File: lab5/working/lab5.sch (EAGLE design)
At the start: 53 parts, among them J1 ISP, U1 ATMEGA128RFA1, Y1 16MHz

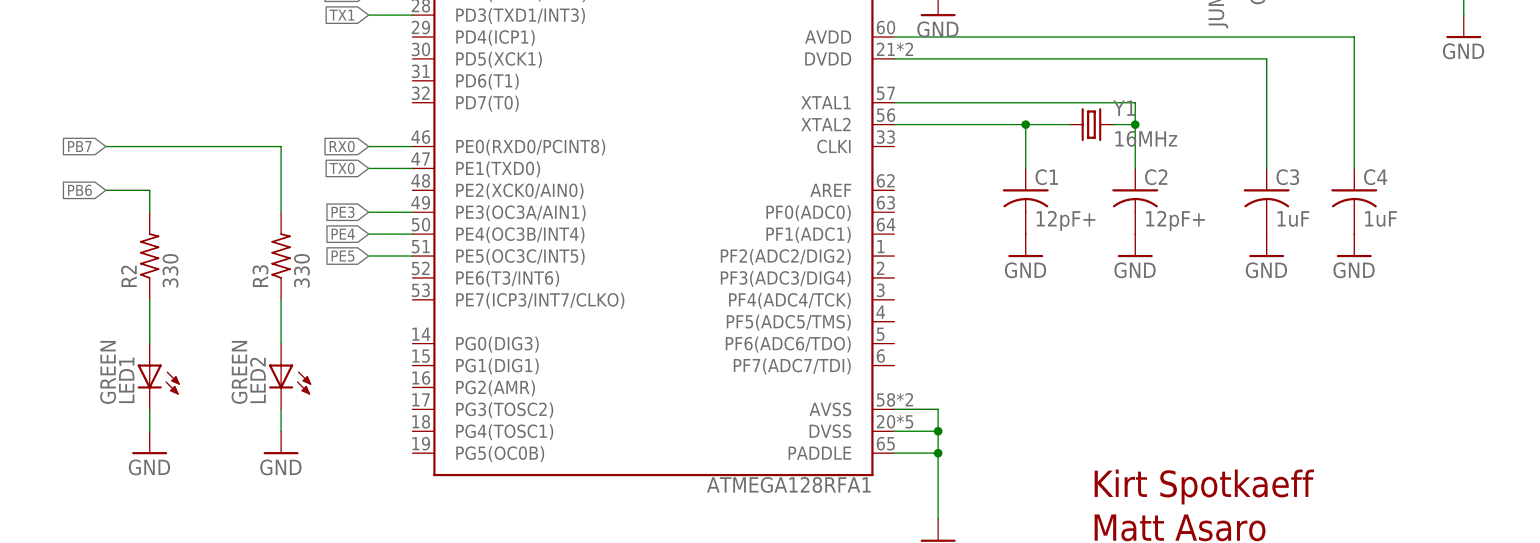
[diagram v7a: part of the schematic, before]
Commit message: updated green led resistor values to 300
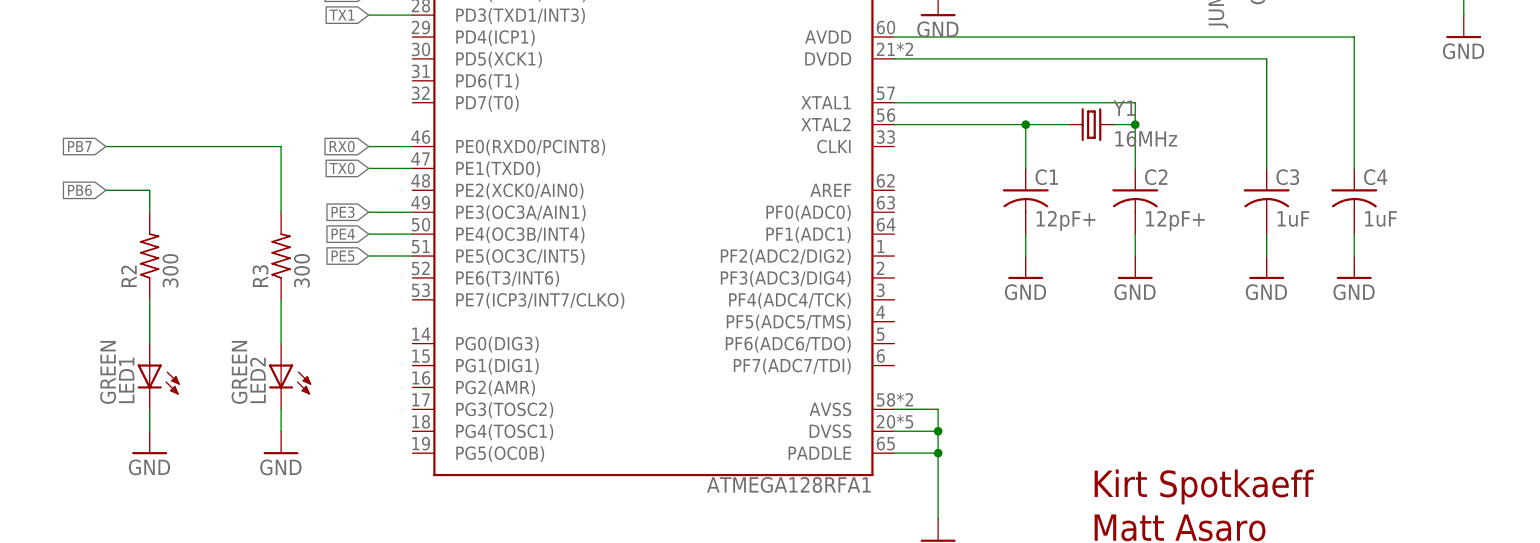
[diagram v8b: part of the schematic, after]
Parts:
- R2, R3: value 330 -> 300
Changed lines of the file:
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@@
 <part name="LED1" library="Lab5" deviceset="LED" device="CHIP-LED0805" value="GREEN"/>
 <part name="LED2" library="Lab5" deviceset="LED" device="CHIP-LED0805" value="GREEN"/>
-<part name="R2" library="Lab5" deviceset="R-US_" device="R0805" value="330"/>
-<part name="R3" library="Lab5" deviceset="R-US_" device="R0805" value="330"/>
+<part name="R2" library="Lab5" deviceset="R-US_" device="R0805" value="300"/>
+<part name="R3" library="Lab5" deviceset="R-US_" device="R0805" value="300"/>
 <part name="GND10" library="Lab5" deviceset="GND" device=""/>
 <part name="GND11" library="Lab5" deviceset="GND" device=""/>
@@
 <instance part="C3" gate="G$1" x="101.6" y="-73.66"/>
 <instance part="C4" gate="G$1" x="111.76" y="-73.66"/>
-<instance part="GND3" gate="1" x="73.66" y="-81.28"/>
-<instance part="GND4" gate="1" x="86.36" y="-81.28"/>
-<instance part="GND5" gate="1" x="101.6" y="-81.28"/>
-<instance part="GND6" gate="1" x="111.76" y="-81.28"/>
+<instance part="GND3" gate="1" x="73.66" y="-83.82"/>
+<instance part="GND4" gate="1" x="86.36" y="-83.82"/>
+<instance part="GND5" gate="1" x="101.6" y="-83.82"/>
+<instance part="GND6" gate="1" x="111.76" y="-83.82"/>
 <instance part="Y1" gate="G$1" x="81.28" y="-66.04"/>
 <instance part="P+1" gate="G$1" x="63.5" y="-15.24"/>
@@
 <pinref part="C1" gate="G$1" pin="2"/>
 <pinref part="GND3" gate="1" pin="GND"/>
+<wire x1="73.66" y1="-81.28" x2="73.66" y2="-78.74" width="0.1524" layer="91"/>
 </segment>
 <segment>
 <pinref part="C2" gate="G$1" pin="2"/>
 <pinref part="GND4" gate="1" pin="GND"/>
+<wire x1="86.36" y1="-81.28" x2="86.36" y2="-78.74" width="0.1524" layer="91"/>
 </segment>
 <segment>
 <pinref part="C3" gate="G$1" pin="2"/>
 <pinref part="GND5" gate="1" pin="GND"/>
+<wire x1="101.6" y1="-81.28" x2="101.6" y2="-78.74" width="0.1524" layer="91"/>
 </segment>
 <segment>
 <pinref part="C4" gate="G$1" pin="2"/>
 <pinref part="GND6" gate="1" pin="GND"/>
-</segment>
-<segment>
+<wire x1="111.76" y1="-81.28" x2="111.76" y2="-78.74" width="0.1524" layer="91"/>
+</segment>
+<segment>
